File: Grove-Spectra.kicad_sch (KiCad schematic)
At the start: 24 parts, among them IC1 PCA9536DP,118, IC2 AS7341-DLGT, IC3 SPX3819M5-L-1-8_TR, J1 114020164, J2 Conn_01x02, Q1 BS250FTA, Q2 BS250FTA, Q3 BS250FTA

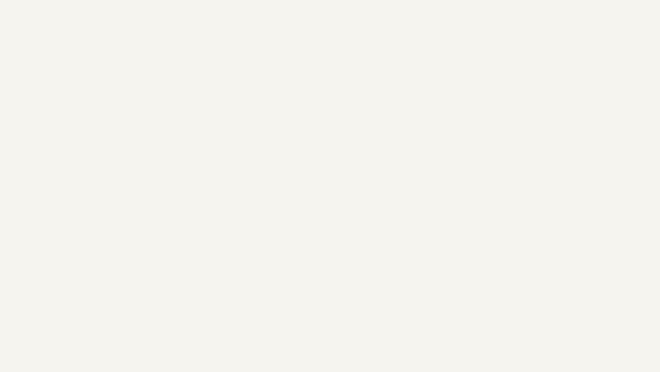
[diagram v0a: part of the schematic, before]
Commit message: Updated for DFA
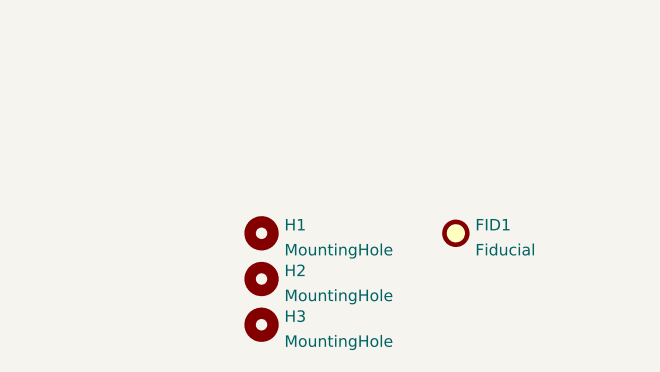
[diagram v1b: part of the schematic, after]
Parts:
- added FID1: Fiducial, personal:Product Stamp, symbol Mechanical:Fiducial
- added H1, H2, H3: MountingHole, MountingHole:MountingHole_2.2mm_M2, symbol Mechanical:MountingHole
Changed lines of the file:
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@@
   (title_block
     (title "Grove Spectrometer")
-    (date "2022-11-15")
+    (date "2022-11-22")
     (rev "A")
   )
@@
     (pin "2")
   )
+  (symbol (lib_id "Mechanical:MountingHole") (at 334.645 238.76 0) (unit 1)
+    (in_bom yes) (on_board yes) (fields_autoplaced)
+    (property "Reference" "H3" (id 0) (at 337.185 237.8515 0)
+      (effects (font (size 1.27 1.27)) (justify left))
+    )
+    (property "Value" "MountingHole" (id 1) (at 337.185 240.6266 0)
+      (effects (font (size 1.27 1.27)) (justify left))
+    )
+    (property "Footprint" "MountingHole:MountingHole_2.2mm_M2" (id 2) (at 334.645 238.76 0)
+      (effects (font (size 1.27 1.27)) hide)
+    )
+    (property "Datasheet" "~" (id 3) (at 334.645 238.76 0)
+      (effects (font (size 1.27 1.27)) hide)
+    )
+  )
   (symbol (lib_id "Capacitor_JLC:100n") (at 179.578 94.488 0) (unit 1)
     (in_bom yes) (on_board yes) (fields_autoplaced)
@@
     (pin "3")
   )
+  (symbol (lib_id "Mechanical:MountingHole") (at 334.645 228.6 0) (unit 1)
+    (in_bom yes) (on_board yes) (fields_autoplaced)
+    (property "Reference" "H1" (id 0) (at 337.185 227.6915 0)
+      (effects (font (size 1.27 1.27)) (justify left))
+    )
+    (property "Value" "MountingHole" (id 1) (at 337.185 230.4666 0)
+      (effects (font (size 1.27 1.27)) (justify left))
+    )
+    (property "Footprint" "MountingHole:MountingHole_2.2mm_M2" (id 2) (at 334.645 228.6 0)
+      (effects (font (size 1.27 1.27)) hide)
+    )
+    (property "Datasheet" "~" (id 3) (at 334.645 228.6 0)
+      (effects (font (size 1.27 1.27)) hide)
+    )
+  )
   (symbol (lib_id "power:+1V8") (at 119.126 162.56 0) (unit 1)
     (in_bom yes) (on_board yes) (fields_autoplaced)
@@
     (pin "2")
   )
+  (symbol (lib_id "Mechanical:Fiducial") (at 356.235 228.6 0) (unit 1)
+    (in_bom yes) (on_board yes) (fields_autoplaced)
+    (property "Reference" "FID1" (id 0) (at 358.394 227.6915 0)
+      (effects (font (size 1.27 1.27)) (justify left))
+    )
+    (property "Value" "Fiducial" (id 1) (at 358.394 230.4666 0)
+      (effects (font (size 1.27 1.27)) (justify left))
+    )
+    (property "Footprint" "personal:Product Stamp" (id 2) (at 356.235 228.6 0)
+      (effects (font (size 1.27 1.27)) hide)
+    )
+    (property "Datasheet" "~" (id 3) (at 356.235 228.6 0)
+      (effects (font (size 1.27 1.27)) hide)
+    )
+  )
   (symbol (lib_id "power:+3V3") (at 105.41 110.236 0) (unit 1)
     (in_bom yes) (on_board yes) (fields_autoplaced)
@@
     (pin "1")
     (pin "2")
+  )
+  (symbol (lib_id "Mechanical:MountingHole") (at 334.645 233.68 0) (unit 1)
+    (in_bom yes) (on_board yes) (fields_autoplaced)
+    (property "Reference" "H2" (id 0) (at 337.185 232.7715 0)
+      (effects (font (size 1.27 1.27)) (justify left))
+    )
+    (property "Value" "MountingHole" (id 1) (at 337.185 235.5466 0)
+      (effects (font (size 1.27 1.27)) (justify left))
+    )
+    (property "Footprint" "MountingHole:MountingHole_2.2mm_M2" (id 2) (at 334.645 233.68 0)
+      (effects (font (size 1.27 1.27)) hide)
+    )
+    (property "Datasheet" "~" (id 3) (at 334.645 233.68 0)
+      (effects (font (size 1.27 1.27)) hide)
+    )
   )
   (symbol (lib_id "Digital_JLC:PCA9536DP,118") (at 200.152 90.424 0) (unit 1)
@@
       (reference "D4") (unit 1) (value "Green_0603") (footprint "LED_SMD:LED_0603_1608Metric")
     )
+    (path "/9d27bec1-8ec1-4630-9bc9-b8dbbfd0db80"
+      (reference "FID1") (unit 1) (value "Fiducial") (footprint "personal:Product Stamp")
+    )
+    (path "/483b8f11-52ae-450a-9324-d9f0c34139f3"
+      (reference "H1") (unit 1) (value "MountingHole") (footprint "MountingHole:MountingHole_2.2mm_M2")
+    )
+    (path "/f5e10107-581d-4cf0-a4ec-0d200fc8359b"
+      (reference "H2") (unit 1) (value "MountingHole") (footprint "MountingHole:MountingHole_2.2mm_M2")
+    )
+    (path "/2dc52309-427e-4ccc-bea0-b10b1df03758"
+      (reference "H3") (unit 1) (value "MountingHole") (footprint "MountingHole:MountingHole_2.2mm_M2")
+    )
     (path "/f7181ad4-ef4a-44cb-8005-5f7deeff8010"
